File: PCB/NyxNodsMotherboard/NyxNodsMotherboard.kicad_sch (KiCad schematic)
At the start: 14 parts, among them J1 2130830005, J2 CPG-04-TH-TR, J3 S2B-PH-SM4-TB_LF__SN_, J4 S2B-PH-SM4-TB_LF__SN_, J5 2130830005, U1 BQ24072TRGTR, U2 TPS62842DGRR

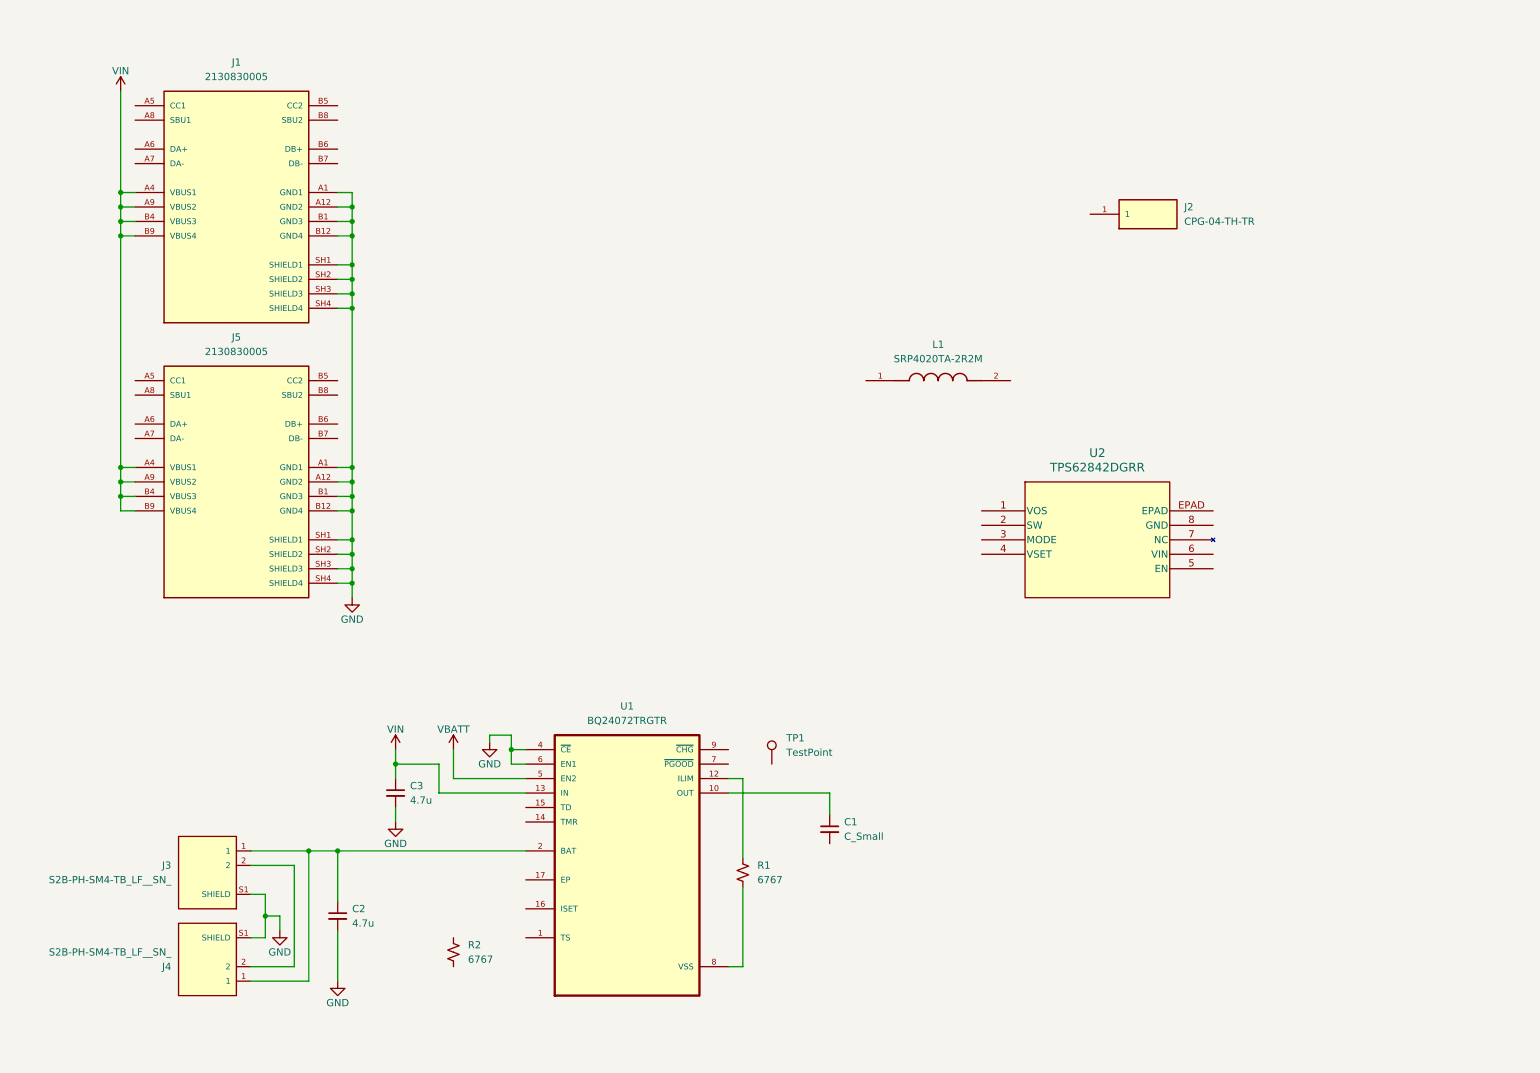
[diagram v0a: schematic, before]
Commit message: Finished battery managment layout
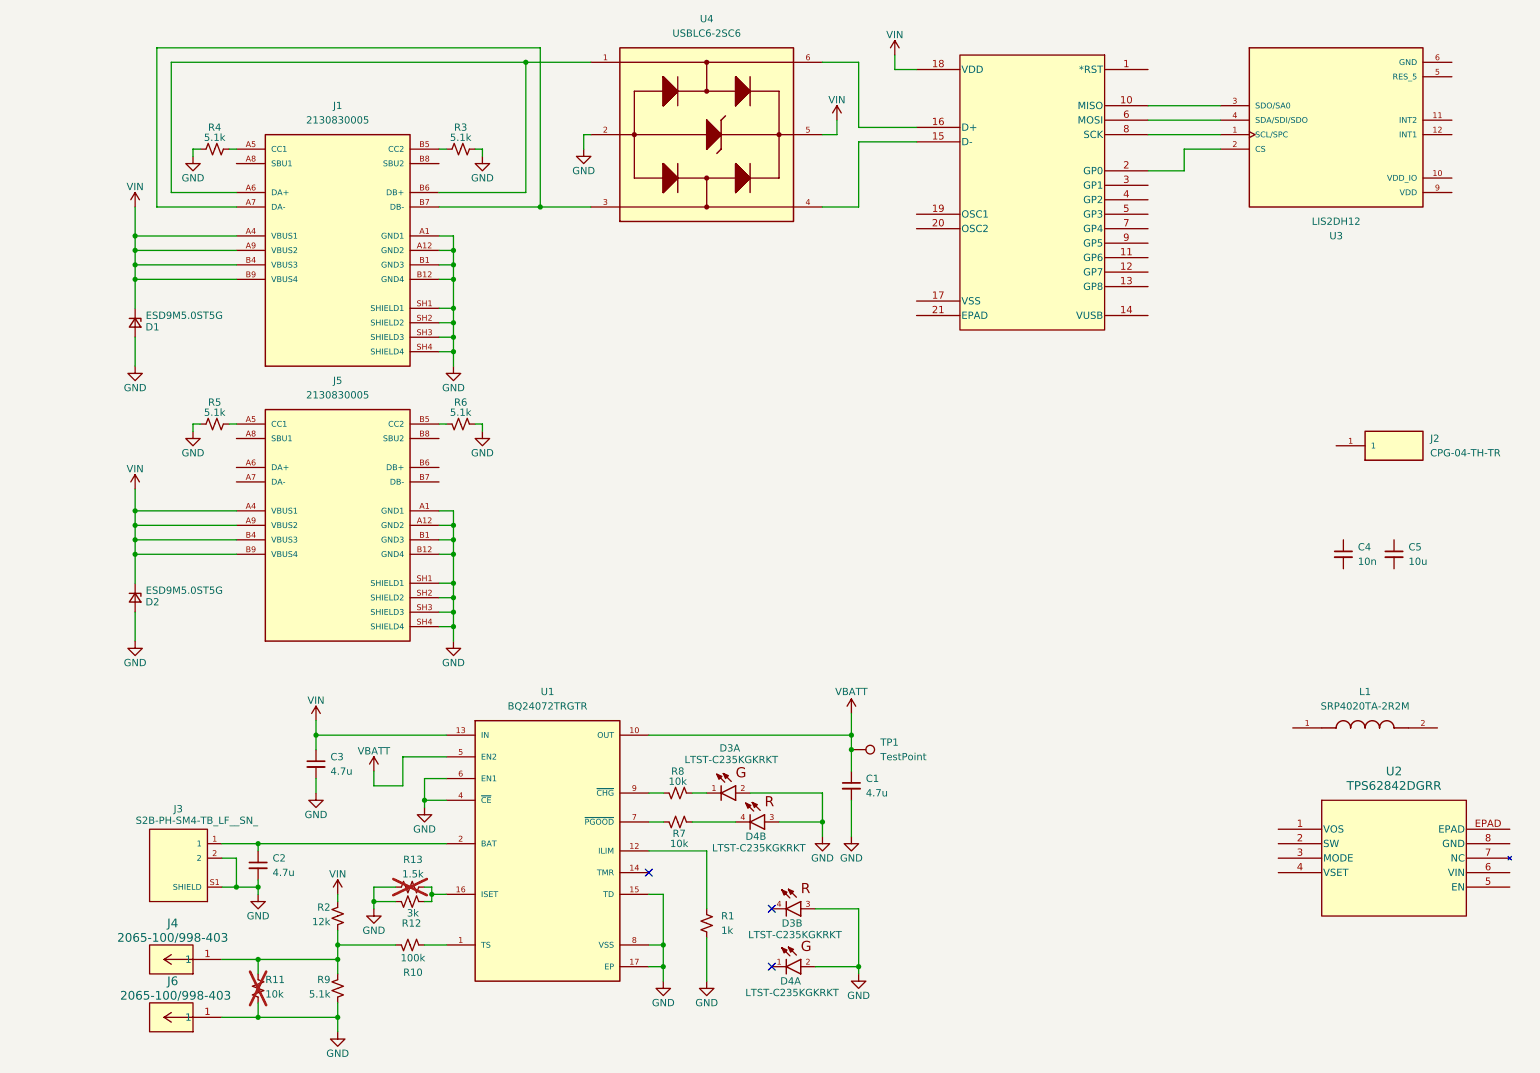
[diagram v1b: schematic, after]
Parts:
- removed J4: S2B-PH-SM4-TB_LF__SN_, S2B-PH-SM4-TB_LF__SN_:JST_S2B-PH-SM4-TB_LF__SN_, symbol NyxNods:S2B-PH-SM4-TB_LF__SN_
- added C4: 10n, symbol Device:C_Small
- added C5: 10u, symbol Device:C_Small
- added D1, D2: ESD9M5.0ST5G, symbol Device:D_Zener_Small
- added D3, D4: LTST-C235KGKRKT, LTST-C235KGKRKT:LED_LTST-C235KGKRKT, symbol NyxNods:LTST-C235KGKRKT
- added J4, J6: 2065-100/998-403, CONN_2065-100/998-403_WAG, symbol NyxNods:2065-100_998-403
- added R10: 100k, symbol Device:R_Small_US
- added R11, R7, R8: 10k, symbol Device:R_Small_US
- added R12: 3k, symbol Device:R_Small_US
- added R13: 1.5k, symbol Device:R_Small_US
- added R3, R4, R5, R6, R9: 5.1k, symbol Device:R_Small_US
- added U3: LIS2DH12, LIS2DH12:SENSOR_LIS2DH12, symbol NyxNods:LIS2DH12
- added U4: USBLC6-2SC6, USBLC6-2SC6:SOT95P280X145-6N, symbol NyxNods:USBLC6-2SC6
- added U5: MCP2210T-I/MQ, QFN20_5x5MC_MCH, symbol NyxNods:MCP2210T-I_MQ
- C1: value C_Small -> 4.7u
- R1: value 6767 -> 1k
- R2: value 6767 -> 12k
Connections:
- net GND: now also C1.2, J3.2, R1.2, U1.15 (TD), U1.17 (EP), U1.8 (VSS), D1.2 (A), D2.2 (A), D3.2, D3.3, D4.2, D4.3, J6.1, R11.2, R12.1, R13.1, R3.2, R4.1, R5.1, R6.1, R9.2, U3.6 (GND), U3.7 (GND), U3.8 (GND), U4.2
- net VBATT: now also C1.1, TP1.1, U1.10 (OUT), U1.11 (OUT)
- net VIN: now also R2.1, D1.1 (K), D2.1 (K), U4.5, U5.18 (VDD)
- net at J5.A5 (CC1): now also R5.2
- net at J5.B5 (CC2): now also R6.2
- net at U1.1 (TS): now also R10.2
- net at U1.16 (ISET): now also R12.2, R13.2
- net at U1.7 (~{PGOOD}): now also R7.2
- net at U1.9 (~{CHG}): now also R8.2
- net at J1.A5 (CC1): now also R4.2
- net at J1.A6 (DA+): now also J1.B6 (DB+), U4.1
- net at J1.A7 (DA-): now also J1.B7 (DB-), U4.3
- net at J1.B5 (CC2): now also R3.1
- net at R2.2: now also J4.1, R10.1, R11.1, R9.1
- new net: U3.3 (SDO/SA0), U5.10 (MISO)
- new net: U4.4, U5.15 (D-)
- new net: U4.6, U5.16 (D+)
- new net: U3.2 (CS), U5.2 (GP0)
- new net: U3.4 (SDA/SDI/SDO), U5.6 (MOSI)
- new net: U3.1 (SCL/SPC), U5.8 (SCK)
- new net: D3.1, R8.1
- new net: D4.4, R7.1
- no-connect marks 0 -> 3
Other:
- moved on the sheet: C2, J1, J2, J3, J5, L1, R2, TP1, U2

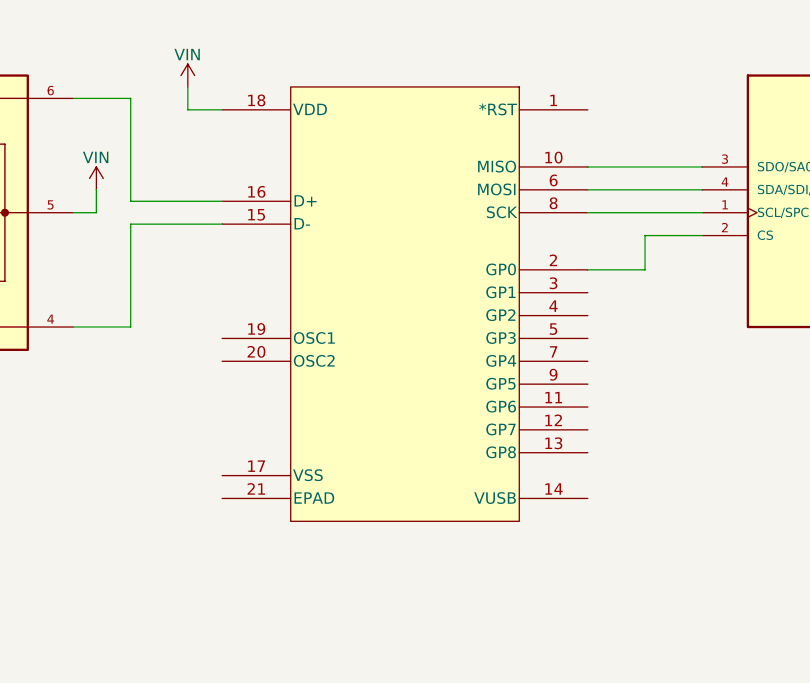
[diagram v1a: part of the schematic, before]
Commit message: Changed my mind to use all analog
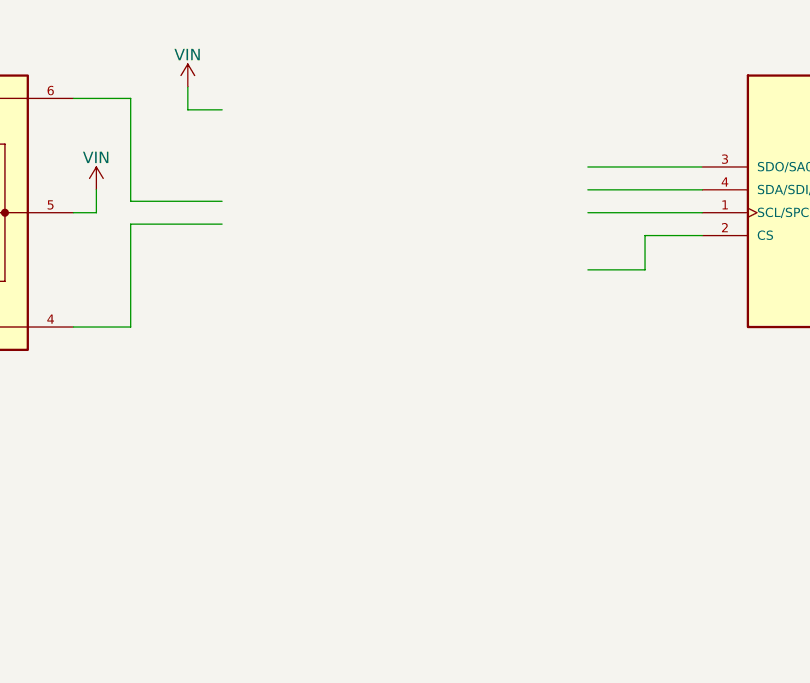
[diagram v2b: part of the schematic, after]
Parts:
- removed U5: MCP2210T-I/MQ, QFN20_5x5MC_MCH, symbol NyxNods:MCP2210T-I_MQ
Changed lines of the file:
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@@
-	)
-	(symbol
-		(lib_id "NyxNods:MCP2210T-I_MQ")
-		(at 198.12 22.86 0)
-		(mirror y)
-		(unit 1)
-		(body_style 1)
-		(exclude_from_sim no)
-		(in_bom yes)
-		(on_board yes)
-		(in_pos_files yes)
-		(dnp no)
-		(fields_autoplaced yes)
-		(property "Reference" "U5"
-			(at 177.8 16.002 0)
-			(hide yes)
-			(show_name no)
-			(do_not_autoplace no)
-			(effects
-				(font
-					(size 1.524 1.524)
-				)
-			)
-		)
-		(property "Value" "MCP2210T-I/MQ"
-			(at 177.8 18.542 0)
-			(hide yes)
-			(show_name no)
-			(do_not_autoplace no)
-			(effects
-				(font
-					(size 1.524 1.524)
-				)
-			)
-		)
-		(property "Footprint" "QFN20_5x5MC_MCH"
-			(at 198.12 22.86 0)
-			(hide yes)
-			(show_name no)
-			(do_not_autoplace no)
-			(effects
-				(font
-					(size 1.27 1.27)
-					(italic yes)
-				)
-			)
-		)
-		(property "Datasheet" "MCP2210T-I/MQ"
-			(at 198.12 22.86 0)
-			(hide yes)
-			(show_name no)
-			(do_not_autoplace no)
-			(effects
-				(font
-					(size 1.27 1.27)
-					(italic yes)
-				)
-			)
-		)
-		(property "Description" ""
-			(at 198.12 22.86 0)
-			(hide yes)
-			(show_name no)
-			(do_not_autoplace no)
-			(effects
-				(font
-					(size 1.27 1.27)
-				)
-			)
-		)
-		(pin "12"
-		)
-		(pin "15"
-		)
-		(pin "13"
-		)
-		(pin "17"
-		)
-		(pin "20"
-		)
-		(pin "14"
-		)
-		(pin "21"
-		)
-		(pin "18"
-		)
-		(pin "16"
-		)
-		(pin "19"
-		)
-		(pin "1"
-		)
-		(pin "6"
-		)
-		(pin "10"
-		)
-		(pin "11"
-		)
-		(pin "4"
-		)
-		(pin "5"
-		)
-		(pin "2"
-		)
-		(pin "3"
-		)
-		(pin "7"
-		)
-		(pin "8"
-		)
-		(pin "9"
-		)
-		(instances
-			(project "NyxNodsMotherboard"
-				(path "/c8aa8e26-5b2f-49b8-a1c0-6e7b3101de21"
-					(reference "U5")
-					(unit 1)
-				)
-			)
-		)
 	)
 	(symbol

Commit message: Battery Schematic
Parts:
- removed U3: LIS2DH12, LIS2DH12:SENSOR_LIS2DH12, symbol NyxNods:LIS2DH12
- removed U4: USBLC6-2SC6, USBLC6-2SC6:SOT95P280X145-6N, symbol NyxNods:USBLC6-2SC6
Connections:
- net at J1.A6 (DA+): no longer J1.B6 (DB+)
- net at J1.A7 (DA-): no longer J1.B7 (DB-)
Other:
- moved on the sheet: C1, C2, C3, C4, C5, D1, D2, D3A, D3B, D4A, D4B, J1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

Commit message: Finished Schematic
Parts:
- removed C4: 10n, symbol Device:C_Small
- removed C5: 10u, symbol Device:C_Small
- added C6: 4.7u, Capacitor_SMD:C_0603_1608Metric, symbol Device:C_Small
- added C7: 10u, Capacitor_SMD:C_0603_1608Metric, symbol Device:C_Small
- added J7: CPG-04-TH-TR, CPG-04-TH-TR:SAMESKY_CPG-04-TH-TR, symbol NyxNods:CPG-04-TH-TR
- added R14: 13k, Resistor_SMD:R_0603_1608Metric, symbol Device:R_Small_US
- added R15: 24k, Resistor_SMD:R_0603_1608Metric, symbol Device:R_Small_US
- added R16, R17: 0, Resistor_SMD:R_0402_1005Metric, symbol Device:R_Small_US
- added TP2: TS, TestPoint:TestPoint_Pad_D2.5mm, symbol Connector:TestPoint
- added TP3: BATT, TestPoint:TestPoint_Pad_D2.5mm, symbol Connector:TestPoint
- added TP4: VIN, TestPoint:TestPoint_Pad_D2.5mm, symbol Connector:TestPoint
- added TP5: GND, TestPoint:TestPoint_Pad_D2.5mm, symbol Connector:TestPoint
- added TP6: SW, TestPoint:TestPoint_Pad_D2.5mm, symbol Connector:TestPoint
- C1, C2, C3: footprint (none) -> Capacitor_SMD:C_0603_1608Metric
- D1, D2: footprint (none) -> Diode_SMD:D_SOD-923
- R1, R10, R2, R3, R4, R5, R6, R7, R8: footprint (none) -> Resistor_SMD:R_0402_1005Metric
- R11, R12, R13, R9: footprint (none) -> Resistor_SMD:R_0603_1608Metric
- TP1: value TestPoint -> VBATT; footprint (none) -> TestPoint:TestPoint_Pad_D2.5mm
- U2: footprint VSSOP_42DGRR_TEX -> NyxNods:VSSOP_42DGRR_TEX
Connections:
- net GND: now also D3.1, D3.4, D4.1, D4.4, U2.3 (MODE), U2.8 (GND), U2.EPAD, C6.2, C7.2, J7.1, R14.2, R15.2, R17.1, TP5.1; no longer D3.2, D3.3, D4.2, D4.3, U1.6 (EN1)
- net VBATT: now also U2.5 (EN), U2.6 (VIN), C6.1, R16.1; no longer U1.5 (EN2)
- net VIN: now also TP4.1
- net at U2.1 (VOS): now also J2.1, L1.2, C7.1
- net at U2.2 (SW): now also L1.1, TP6.1
- net at U2.4 (VSET): now also R14.1, R15.1
- net at R8.1: now also D4.3; no longer D3.1
- net at R10.2, U1.1 (TS): now also TP2.1
- net at C2.1, J3.1, U1.2 (BAT)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: now also TP3.1
- net at R7.1: now also D3.2; no longer D4.4
- new net: R16.2, U1.5 (EN2)
- new net: R17.2, U1.6 (EN1)
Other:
- moved on the sheet: C3, L1

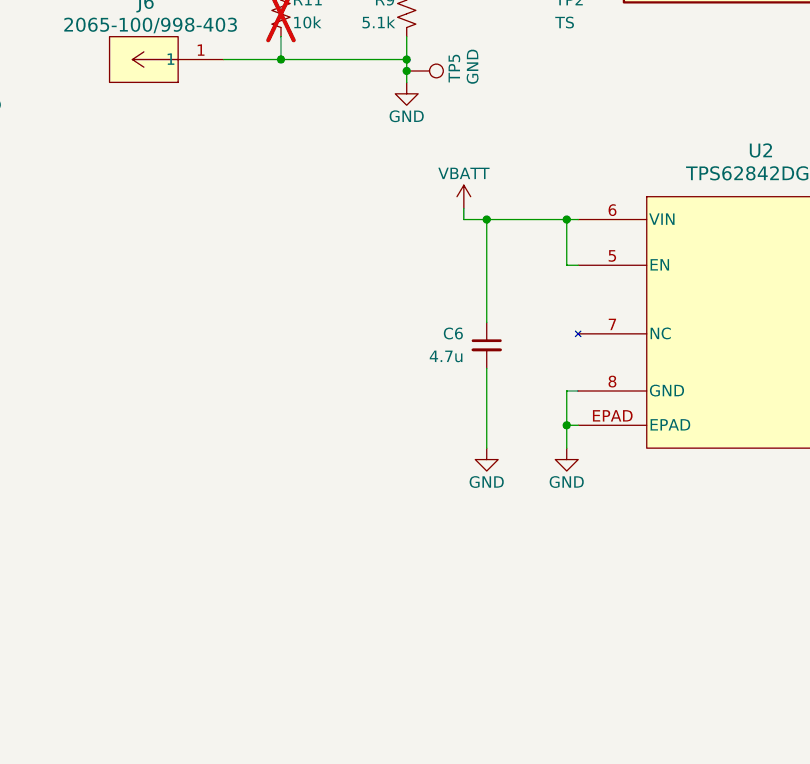
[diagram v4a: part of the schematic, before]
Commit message: Updated with button
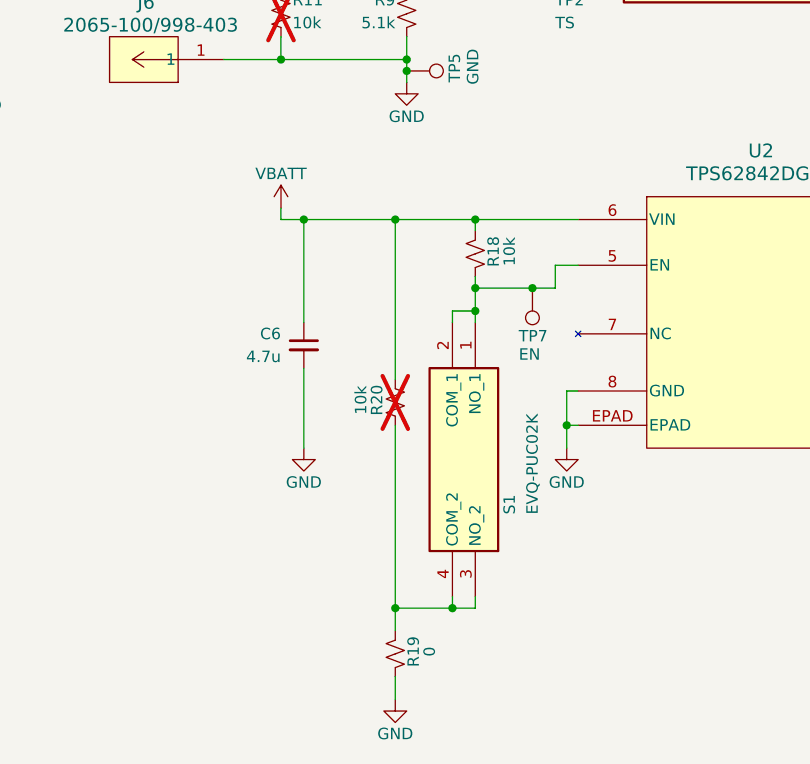
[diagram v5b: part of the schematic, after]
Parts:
- added R18, R20: 10k, Resistor_SMD:R_0402_1005Metric, symbol Device:R_Small_US
- added R19: 0, Resistor_SMD:R_0402_1005Metric, symbol Device:R_Small_US
- added S1: EVQ-PUC02K, NyxNods:EVQPUC02K, symbol NyxNods:EVQ-PUC02K
- added TP7: EN, TestPoint:TestPoint_Pad_D2.5mm, symbol Connector:TestPoint
- D3, D4: footprint LTST-C235KGKRKT:LED_LTST-C235KGKRKT -> NyxNods:LED_LTST-C235KGKRKT
- J1, J5: footprint 2130830005:MOLEX_2130830005 -> NyxNods:MOLEX_2130830005
- J2, J7: footprint CPG-04-TH-TR:SAMESKY_CPG-04-TH-TR -> NyxNods:SAMESKY_CPG-04-TH-TR
- J3: footprint S2B-PH-SM4-TB_LF__SN_:JST_S2B-PH-SM4-TB_LF__SN_ -> NyxNods:JST_S2B-PH-SM4-TB_LF__SN_
- J4, J6: footprint CONN_2065-100/998-403_WAG -> NyxNods:CONN_2065-100&slash_998-403_WAG
- L1: footprint SRP4020TA-2R2M:IND_SRP4020TA-2R2M -> NyxNods:IND_SRP4020TA-2R2M
- U1: footprint BQ24072TRGTR:QFN50P300X300X100-17N -> NyxNods:QFN50P300X300X100-17N
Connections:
- net GND: now also R19.2
- net VBATT: now also R18.1, R20.1; no longer U2.5 (EN)
- new net: R18.2, S1.1 (NO_1), S1.2 (COM_1), TP7.1, U2.5 (EN)
- new net: R19.1, R20.2, S1.3 (NO_2), S1.4 (COM_2)
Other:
- moved on the sheet: C6

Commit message: Started Layout
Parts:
- added H1, H2, H3, H4: MountingHole, NyxNods:MountingHole_1.8mm_M1.6_ISO14580_Pad_TopBottom, symbol Mechanical:MountingHole
- C1, C2, C3, C6, C7: footprint Capacitor_SMD:C_0603_1608Metric -> Capacitor_SMD:C_0402_1005Metric
- R11, R12, R13, R14, R15, R9: footprint Resistor_SMD:R_0603_1608Metric -> Resistor_SMD:R_0402_1005Metric
- TP1, TP2, TP3, TP4, TP5, TP6, TP7: footprint TestPoint:TestPoint_Pad_D2.5mm -> TestPoint:TestPoint_Pad_D1.0mm
